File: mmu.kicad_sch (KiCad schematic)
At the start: 33 parts, among them Q1 DMG1012TQ-7, U1 74LVC245ABQ,115, U2 74LVC245ABQ,115, U3 ICE5LP1K-SG48ITR, U4 74LVC245ABQ,115, U5 MIC5504-3.3YM5-TR, U6 MIC5365-1.2YC5-TR, U8 W25X20CLUXIG_TR

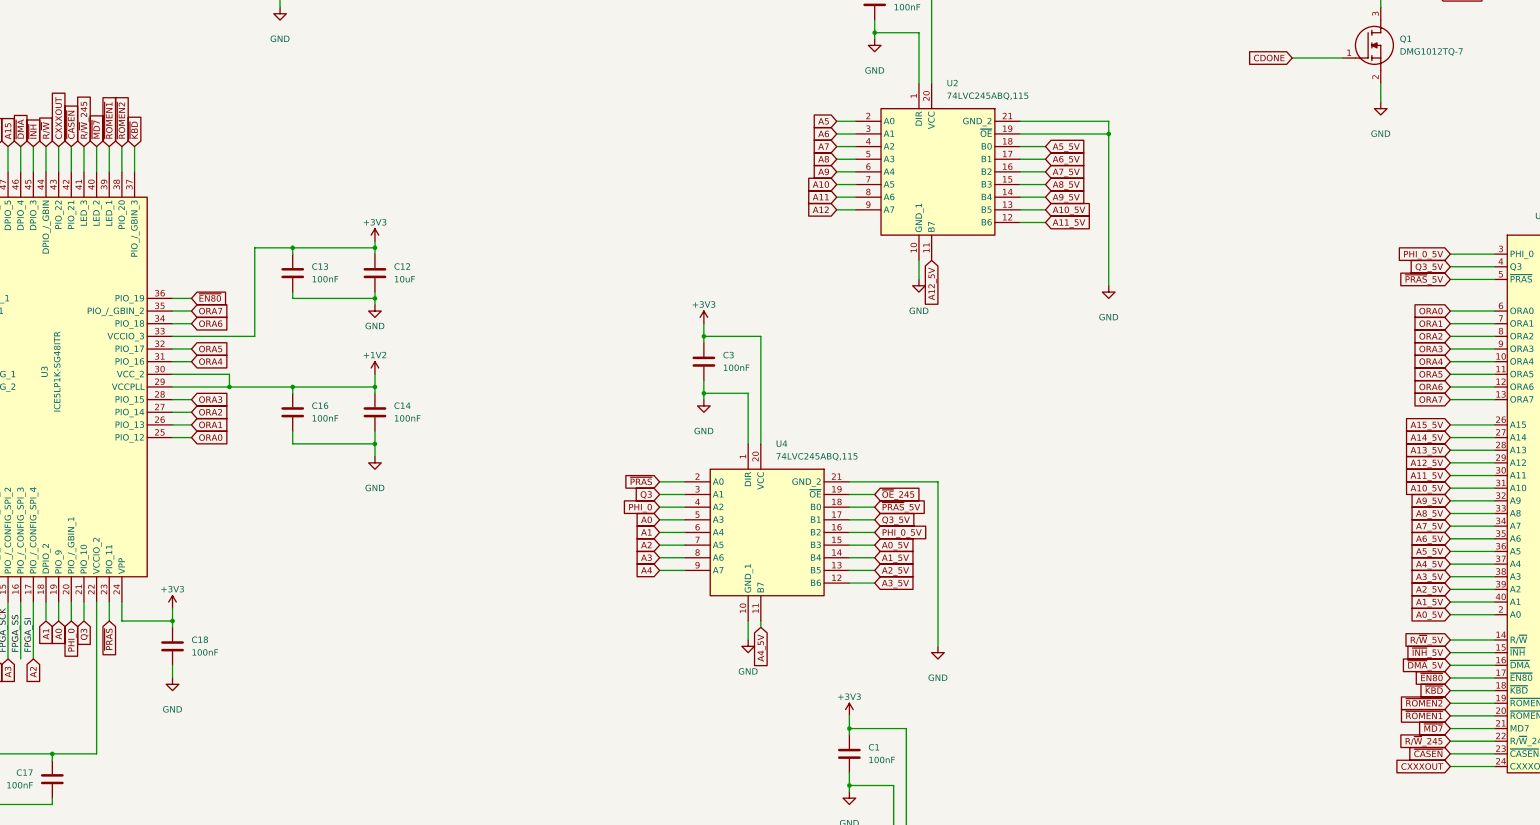
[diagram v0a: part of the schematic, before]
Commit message: Added untested MMU firmware
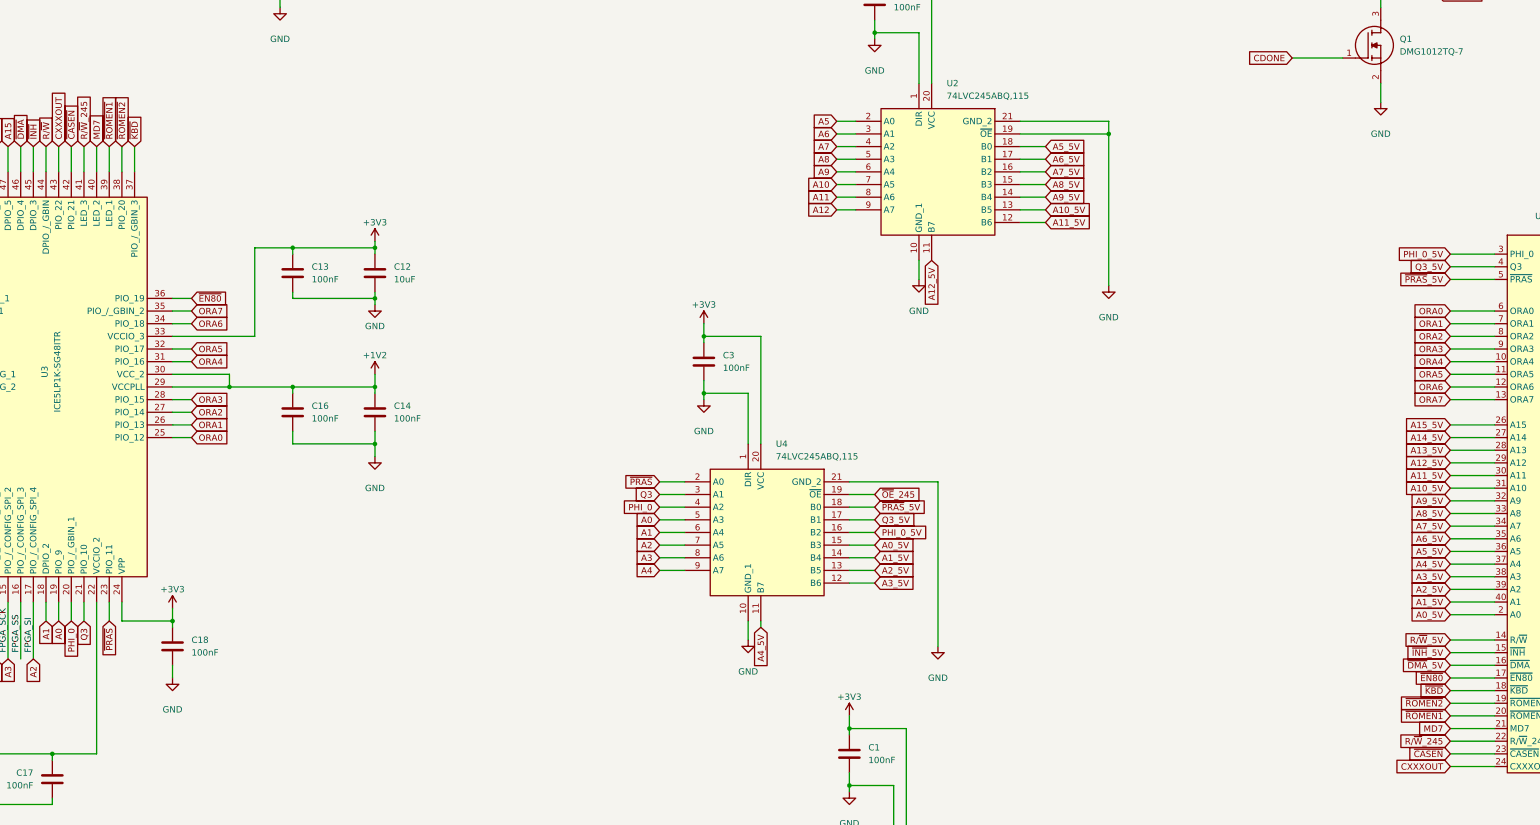
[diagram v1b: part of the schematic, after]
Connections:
- net ~{MD7} renamed MD7
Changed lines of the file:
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@@
 	(title_block
 		(title "Apple IIe IOU Replacement")
-		(date "2024-12-10")
-		(rev "0.90")
+		(date "2025-01-10")
+		(rev "0.95")
 		(company "Frozen Signal")
 	)
@@
 		)
 	)
-	(global_label "~{MD7}"
+	(global_label "MD7"
 		(shape input)
 		(at 373.38 193.04 180)
@@
 		)
 	)
-	(global_label "~{MD7}"
+	(global_label "MD7"
 		(shape input)
 		(at 101.6 76.2 90)

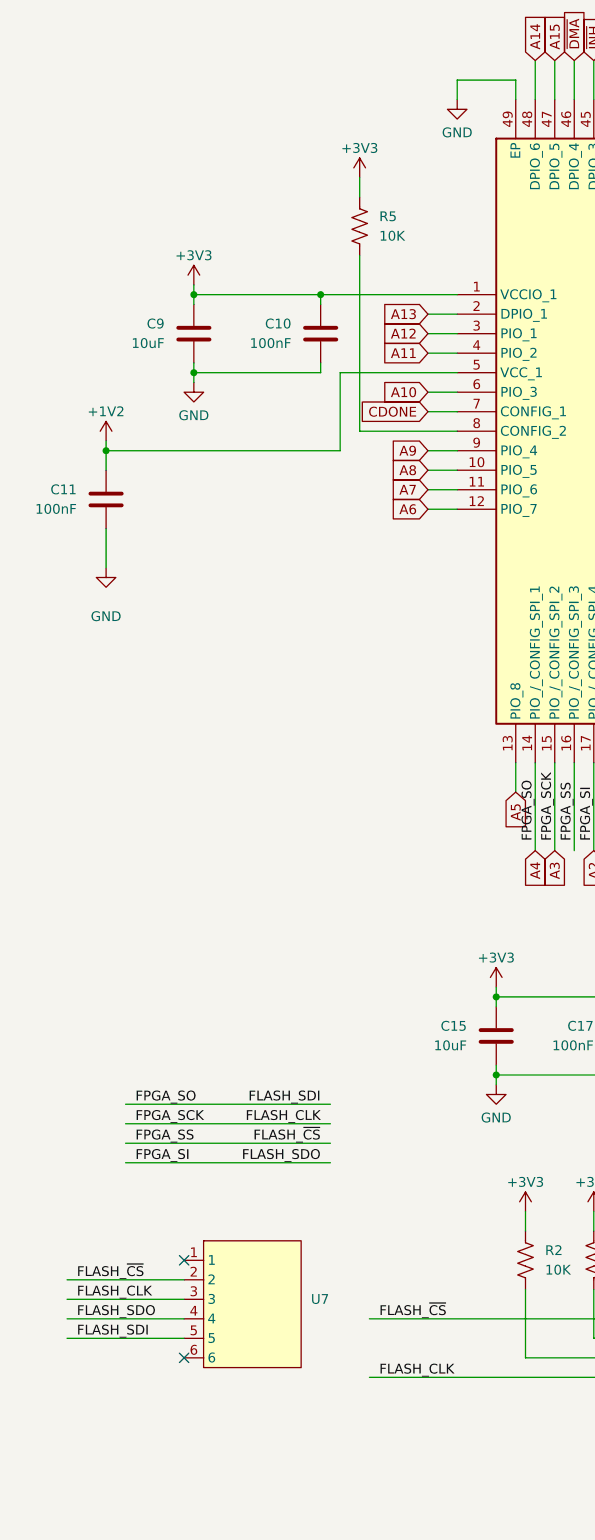
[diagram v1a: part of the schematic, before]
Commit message: Changed programming connector to a TC2050
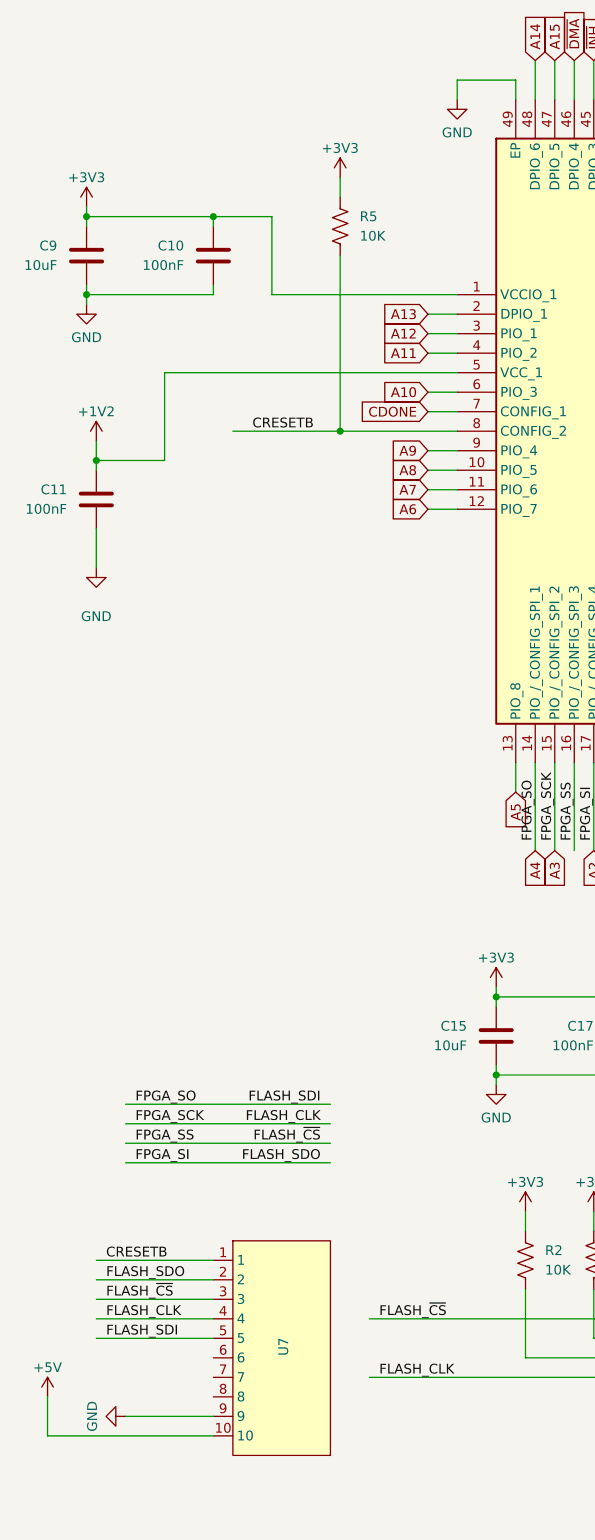
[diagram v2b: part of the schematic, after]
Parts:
- U1, U2, U4: footprint 000_Footprints:74LVC245ABQ115 -> 74LVC245ABQ115
- U7: footprint Connector:Tag-Connect_TC2030-IDC-NL_2x03_P1.27mm_Vertical -> 000_Footprints:Tag-Connect_TC2050-IDC-NL_2x05_P1.27mm_Vertical
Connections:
- net +5V: now also U7.10
- net A2: now also U7.2; no longer U7.4
- net A3: now also U7.4; no longer U7.3
- net FLASH_~{CS}: now also U7.3; no longer U7.2
- net GND: now also U7.9
- net CRESETB: now reaches U7.1
- net CRESETB: now also R5.2, U3.8 (CONFIG_2)
- no-connect marks 3 -> 1
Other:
- moved on the sheet: C10, C11, C9, R5

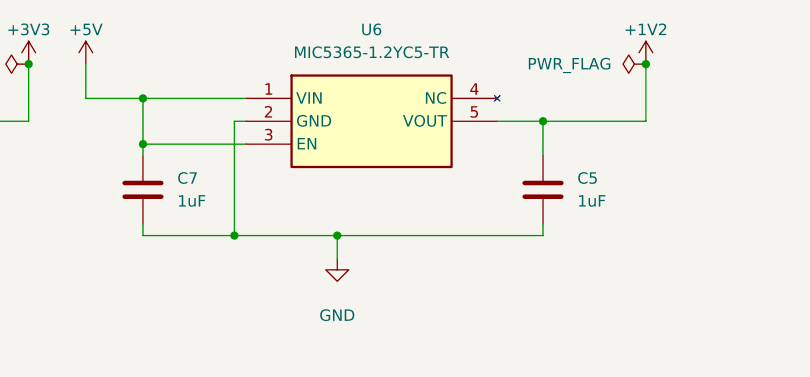
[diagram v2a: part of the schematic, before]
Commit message: Changed the 1.2V LDO & other small changes (#5)
* small changes

* Changed the 3.3V LDO
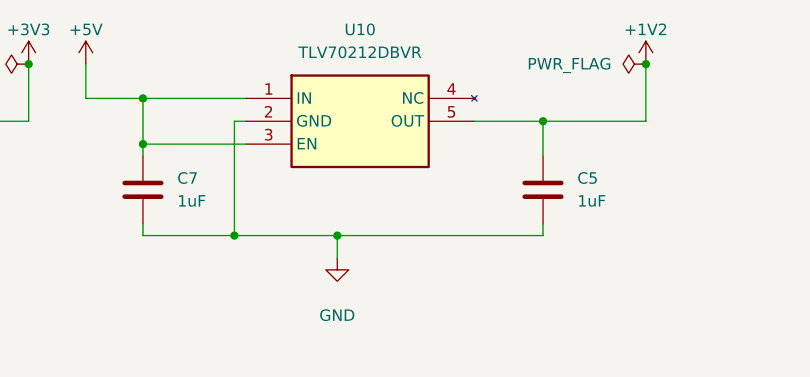
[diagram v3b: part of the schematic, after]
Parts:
- removed U6: MIC5365-1.2YC5-TR, 000_Footprints:SOT65P210X110-5N, symbol 000_Symbols:MIC5365-1.2YC5-TR
- added U10: TLV70212DBVR, 000_Footprints:SOT95P280X145-5N, symbol 000_Symbols:TLV70212DBVR
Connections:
- net +1V2: now also U10.5 (OUT)
- net +5V: now also U10.1 (IN), U10.3 (EN)
- net GND: now also U10.2 (GND)
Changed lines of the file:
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@@
 	(wire
 		(pts
+			(xy 153.67 33.02) (xy 161.29 33.02)
+		)
+		(stroke
+			(width 0)
+			(type default)
+		)
+	)
+	(wire
+		(pts
 			(xy 134.62 245.11) (xy 144.78 245.11)
 		)
@@
 	(wire
 		(pts
-			(xy 156.21 33.02) (xy 161.29 33.02)
-		)
-		(stroke
-			(width 0)
-			(type default)
-		)
-	)
-	(wire
-		(pts
 			(xy 243.84 222.25) (xy 248.92 222.25)
 		)
@@
 	)
 	(symbol
-		(lib_id "000_Symbols:MIC5365-1.2YC5-TR")
-		(at 128.27 30.48 0)
-		(unit 1)
-		(exclude_from_sim no)
-		(in_bom yes)
-		(on_board yes)
-		(dnp no)
-		(fields_autoplaced yes)
-		(property "Reference" "U6"
-			(at 142.24 22.86 0)
-			(effects
-				(font
-					(size 1.27 1.27)
-				)
-			)
-		)
-		(property "Value" "MIC5365-1.2YC5-TR"
-			(at 142.24 25.4 0)
-			(effects
-				(font
-					(size 1.27 1.27)
-				)
-			)
-		)
-		(property "Footprint" "000_Footprints:SOT65P210X110-5N"
-			(at 152.4 125.4 0)
-			(effects
-				(font
-					(size 1.27 1.27)
-				)
-				(justify left top)
-				(hide yes)
-			)
-		)
-		(property "Datasheet" "http://www.microchip.com/mymicrochip/filehandler.aspx?ddocname=en580022"
-			(at 152.4 225.4 0)
-			(effects
-				(font
-					(size 1.27 1.27)
-				)
-				(justify left top)
-				(hide yes)
-			)
-		)
-		(property "Description" "LDO Voltage Regulators Ultra Small Single 150mA LDO"
-			(at 128.27 30.48 0)
-			(effects
-				(font
-					(size 1.27 1.27)
-				)
-				(hide yes)
-			)
-		)
-		(pin "5"
-		)
-		(pin "3"
-		)
-		(pin "1"
-		)
-		(pin "2"
-		)
-		(pin "4"
-		)
-		(instances
-			(project ""
-				(path "/55069440-6249-4c38-b942-beed3e8959d4/f9912975-c562-40c0-85ff-d613bdd8ed9a"
-					(reference "U6")
-					(unit 1)
-				)
-			)
-		)
-	)
-	(symbol
 		(lib_id "power:+5V")
 		(at 110.49 26.67 0)
@@
 					(unit 1)
 				)
+			)
+		)
+	)
+	(symbol
+		(lib_id "000_Symbols:TLV70212DBVR")
+		(at 128.27 30.48 0)
+		(unit 1)
+		(exclude_from_sim no)
+		(in_bom yes)
+		(on_board yes)
+		(dnp no)
+		(fields_autoplaced yes)
+		(property "Reference" "U10"
+			(at 140.97 22.86 0)
+			(effects
+				(font
+					(size 1.27 1.27)
+				)
+			)
+		)
+		(property "Value" "TLV70212DBVR"
+			(at 140.97 25.4 0)
+			(effects
+				(font
+					(size 1.27 1.27)
+				)
+			)
+		)
+		(property "Footprint" "000_Footprints:SOT95P280X145-5N"
+			(at 149.86 125.4 0)
+			(effects
+				(font
+					(size 1.27 1.27)
+				)
+				(justify left top)
+				(hide yes)
+			)
+		)
+		(property "Datasheet" "http://www.ti.com/lit/gpn/tlv702"
+			(at 149.86 225.4 0)
+			(effects
+				(font
+					(size 1.27 1.27)
+				)
+				(justify left top)
+				(hide yes)
+			)
+		)
+		(property "Description" "300mA Low-Iq Low-Dropout (LDO) Regulator for Portables"
+			(at 128.27 30.48 0)
+			(effects
+				(font
+					(size 1.27 1.27)
+				)
+				(hide yes)
+			)
+		)
+		(property "Height" "1.45"
+			(at 149.86 425.4 0)
+			(effects
+				(font
+					(size 1.27 1.27)
+				)
+				(justify left top)
+				(hide yes)
+			)
+		)
+		(property "Mouser Part Number" "595-TLV70212DBVR"
+			(at 149.86 525.4 0)
+			(effects
+				(font
+					(size 1.27 1.27)
+				)
+				(justify left top)
+				(hide yes)
+			)
+		)
+		(property "Mouser Price/Stock" "https://www.mouser.co.uk/ProductDetail/Texas-Instruments/TLV70212DBVR?qs=O1HRStiETChPj4iJQTN0bg%3D%3D"
+			(at 149.86 625.4 0)
+			(effects
+				(font
+					(size 1.27 1.27)
+				)
+				(justify left top)
+				(hide yes)
+			)
+		)
+		(property "Manufacturer_Name" "Texas Instruments"
+			(at 149.86 725.4 0)
+			(effects
+				(font
+					(size 1.27 1.27)
+				)
+				(justify left top)
+				(hide yes)
+			)
+		)
+		(property "Manufacturer_Part_Number" "TLV70212DBVR"
+			(at 149.86 825.4 0)
+			(effects
+				(font
+					(size 1.27 1.27)
+				)
+				(justify left top)
+				(hide yes)
+			)
+		)
+		(property "JCL" "C81462"
+			(at 128.27 30.48 0)
+			(effects
+				(font
+					(size 1.27 1.27)
+				)
+				(hide yes)
+			)
+		)
+		(property "Field11" ""
+			(at 128.27 30.48 0)
+			(effects
+				(font
+					(size 1.27 1.27)
+				)
+				(hide yes)
+			)
+		)
+		(pin "1"
+		)
+		(pin "4"
+		)
+		(pin "3"
+		)
+		(pin "2"
+		)
+		(pin "5"
+		)
+		(instances
+			(project ""
+				(path "/55069440-6249-4c38-b942-beed3e8959d4/f9912975-c562-40c0-85ff-d613bdd8ed9a"
+					(reference "U10")
+					(unit 1)
+				)
